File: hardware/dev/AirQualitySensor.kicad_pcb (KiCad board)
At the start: 2 copper layers, 81.3 x 36.8 mm, 44 parts, among them J1 USB_C_Receptacle_USB2.0, J2 SWD, J3 UART, U1 004-0-0053, U2 DHT22, U3 XC6206P332MR

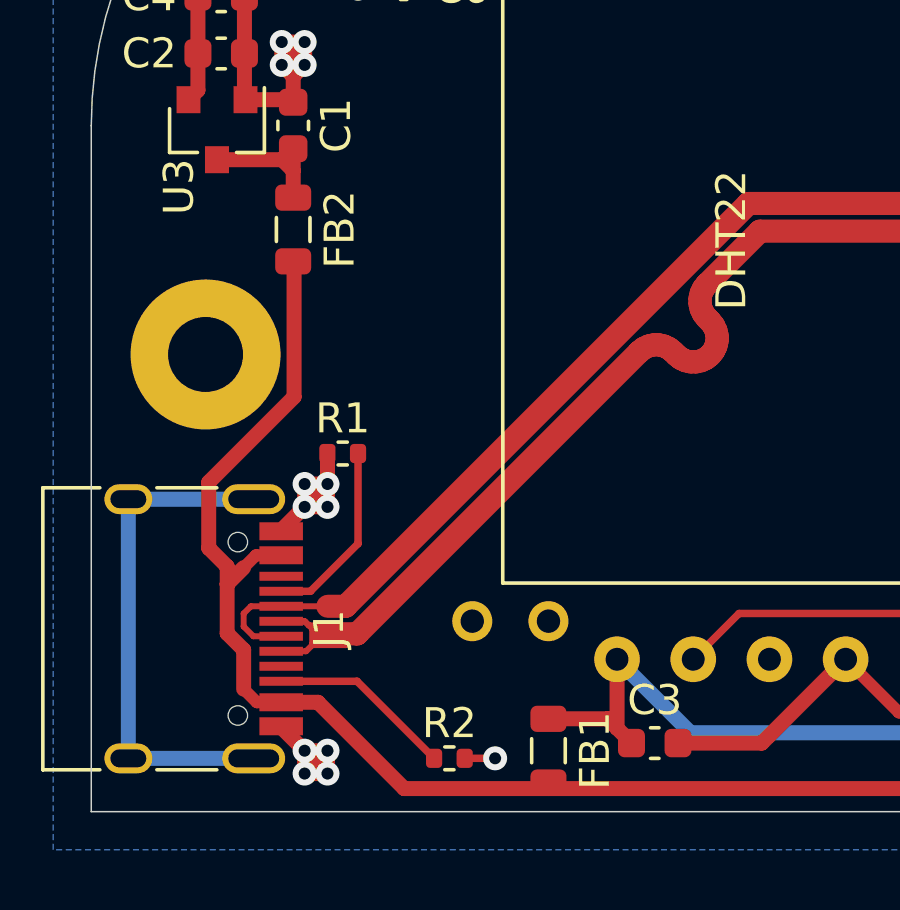
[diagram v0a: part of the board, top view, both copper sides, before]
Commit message: Fix inductor footprint
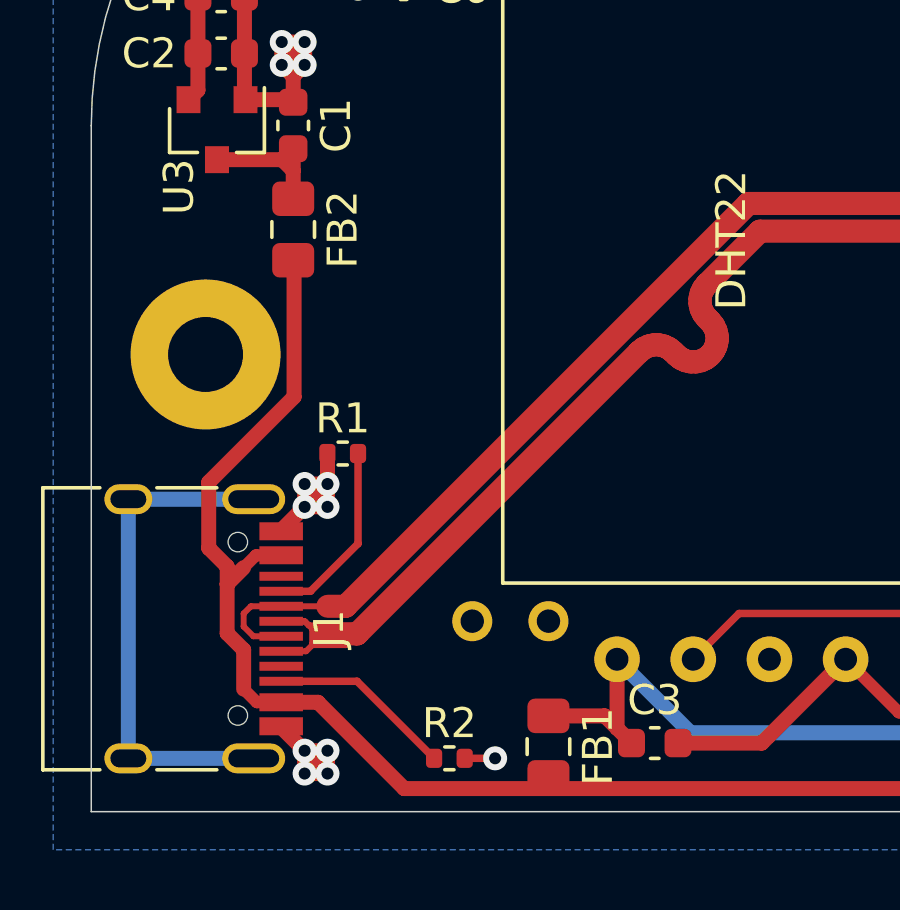
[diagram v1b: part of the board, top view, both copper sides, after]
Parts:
- FB1, FB2: footprint Inductor_SMD:L_0805_2012Metric -> Inductor_SMD:L_0805_2012Metric_Pad1.15x1.40mm_HandSolder
- moved FB1 0.14 mm to (121.9, 119.8)

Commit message: Fix flipped red-green LEDs
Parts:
- D1: value Red -> Green
- D3: value Green -> Red
- R6: value 10k -> 100k
- R8: value 100k -> 10k
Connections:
- A1 pad 7: LED_GREEN -> LED_RED
- A1 pad 9: LED_RED -> LED_GREEN
- R6 pad 2: LED_RED -> LED_GREEN
- R8 pad 2: LED_GREEN -> LED_RED
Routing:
- net LED_RED: track 12.5 -> 19.0 mm
- net LED_GREEN: track 19.0 -> 12.5 mm
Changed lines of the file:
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@@
   )
   (setup
-    (last_trace_width 0.5)
+    (last_trace_width 0.25)
     (user_trace_width 0.4)
     (user_trace_width 0.5)
@@
       (effects (font (size 1 1) (thickness 0.15)))
     )
-    (fp_text user %R (at 0 0 90) (layer F.Fab)
-      (effects (font (size 0.5 0.5) (thickness 0.08)))
-    )
     (fp_line (start -1 0.6) (end -1 -0.6) (layer F.Fab) (width 0.1))
     (fp_line (start -1 -0.6) (end 1 -0.6) (layer F.Fab) (width 0.1))
@@
     (fp_line (start 1.85 -0.95) (end 1.85 0.95) (layer F.CrtYd) (width 0.05))
     (fp_line (start 1.85 0.95) (end -1.85 0.95) (layer F.CrtYd) (width 0.05))
+    (fp_text user %R (at 0 0 90) (layer F.Fab)
+      (effects (font (size 0.5 0.5) (thickness 0.08)))
+    )
     (pad 2 smd roundrect (at 1.025 0 270) (size 1.15 1.4) (layers F.Cu F.Paste F.Mask) (roundrect_rratio 0.217391)
       (net 26 VBUS))
@@
     (fp_text value 100R (at 0 1.65 90) (layer F.Fab)
       (effects (font (size 1 1) (thickness 0.15)))
-    )
-    (fp_text user %R (at 0 0 90) (layer F.Fab)
-      (effects (font (size 0.5 0.5) (thickness 0.08)))
     )
     (fp_line (start -1 0.6) (end -1 -0.6) (layer F.Fab) (width 0.1))
@@
     (fp_line (start 1.85 -0.95) (end 1.85 0.95) (layer F.CrtYd) (width 0.05))
     (fp_line (start 1.85 0.95) (end -1.85 0.95) (layer F.CrtYd) (width 0.05))
+    (fp_text user %R (at 0 0 90) (layer F.Fab)
+      (effects (font (size 0.5 0.5) (thickness 0.08)))
+    )
     (pad 2 smd roundrect (at 1.025 0 270) (size 1.15 1.4) (layers F.Cu F.Paste F.Mask) (roundrect_rratio 0.217391)
       (net 26 VBUS))
@@
       (effects (font (size 1 1) (thickness 0.15)))
     )
-    (fp_text value 100k (at 0 1.17 90) (layer F.Fab)
+    (fp_text value 10k (at 0 1.17 90) (layer F.Fab)
       (effects (font (size 1 1) (thickness 0.15)))
     )
@@
     )
     (pad 2 smd roundrect (at 0.51 0 270) (size 0.54 0.64) (layers F.Cu F.Paste F.Mask) (roundrect_rratio 0.25)
-      (net 55 LED_GREEN))
+      (net 53 LED_RED))
     (pad 1 smd roundrect (at -0.51 0 270) (size 0.54 0.64) (layers F.Cu F.Paste F.Mask) (roundrect_rratio 0.25)
       (net 61 "Net-(D3-Pad2)"))
@@
       (effects (font (size 1 1) (thickness 0.15)))
     )
-    (fp_text value 10k (at 0 1.17 90) (layer F.Fab)
+    (fp_text value 100k (at 0 1.17 90) (layer F.Fab)
       (effects (font (size 1 1) (thickness 0.15)))
     )
@@
     )
     (pad 2 smd roundrect (at 0.51 0 270) (size 0.54 0.64) (layers F.Cu F.Paste F.Mask) (roundrect_rratio 0.25)
-      (net 53 LED_RED))
+      (net 55 LED_GREEN))
     (pad 1 smd roundrect (at -0.51 0 270) (size 0.54 0.64) (layers F.Cu F.Paste F.Mask) (roundrect_rratio 0.25)
       (net 59 "Net-(D1-Pad2)"))
@@
       (effects (font (size 1 1) (thickness 0.15)) (justify mirror))
     )
-    (fp_text value Green (at 1.27 -2.96 -90) (layer B.Fab)
+    (fp_text value Red (at 1.27 -2.96 -90) (layer B.Fab)
       (effects (font (size 1 1) (thickness 0.15)) (justify mirror))
     )
@@
       (effects (font (size 1 1) (thickness 0.15)) (justify mirror))
     )
-    (fp_text value Red (at 1.27 -2.96 -90) (layer B.Fab)
+    (fp_text value Green (at 1.27 -2.96 -90) (layer B.Fab)
       (effects (font (size 1 1) (thickness 0.15)) (justify mirror))
     )
@@
       (net 70 LED_STATUS0))
     (pad 9 smd roundrect (at -6.75 2.2 180) (size 1.53 0.67) (layers F.Cu F.Paste F.Mask) (roundrect_rratio 0.25)
-      (net 53 LED_RED))
+      (net 55 LED_GREEN))
     (pad 8 smd roundrect (at -6.75 1.1 180) (size 1.53 0.67) (layers F.Cu F.Paste F.Mask) (roundrect_rratio 0.25)
       (net 54 LED_YELLOW))
@@
       (net 48 SWD_SWCLK))
     (pad 7 smd roundrect (at -6.75 0 180) (size 1.53 0.67) (layers F.Cu F.Paste F.Mask) (roundrect_rratio 0.25)
-      (net 55 LED_GREEN))
+      (net 53 LED_RED))
   )
   (gr_text "PCB ID:" (at 133.35 109.22) (layer B.SilkS)
@@
   (segment (start 159.757553 114.590999) (end 155.214003 114.590999) (width 0.25) (layer F.Cu) (net 51))
   (segment (start 160.532 115.316) (end 160.482554 115.316) (width 0.25) (layer F.Cu) (net 51))
-  (via (at 150.368 100.076) (size 0.8) (drill 0.4) (layers F.Cu B.Cu) (net 53))
-  (segment (start 150.368 100.076) (end 150.368 99.062) (width 0.25) (layer F.Cu) (net 53))
-  (via (at 152.527 108.204) (size 0.8) (drill 0.4) (layers F.Cu B.Cu) (net 53))
-  (segment (start 151.482685 109.814) (end 151.022 109.814) (width 0.25) (layer F.Cu) (net 53))
-  (segment (start 152.527 108.769685) (end 151.482685 109.814) (width 0.25) (layer F.Cu) (net 53))
-  (segment (start 152.527 108.204) (end 152.527 108.769685) (width 0.25) (layer F.Cu) (net 53))
-  (segment (start 150.368 106.045) (end 150.368 100.076) (width 0.25) (layer B.Cu) (net 53))
-  (segment (start 152.527 108.204) (end 150.368 106.045) (width 0.25) (layer B.Cu) (net 53))
+  (via (at 150.368 100.076) (size 0.8) (drill 0.4) (layers F.Cu B.Cu) (net 55))
+  (segment (start 150.368 100.076) (end 150.368 99.062) (width 0.25) (layer F.Cu) (net 55))
+  (via (at 152.527 108.204) (size 0.8) (drill 0.4) (layers F.Cu B.Cu) (net 55))
+  (segment (start 151.482685 109.814) (end 151.022 109.814) (width 0.25) (layer F.Cu) (net 55))
+  (segment (start 152.527 108.769685) (end 151.482685 109.814) (width 0.25) (layer F.Cu) (net 55))
+  (segment (start 152.527 108.204) (end 152.527 108.769685) (width 0.25) (layer F.Cu) (net 55))
+  (segment (start 150.368 106.045) (end 150.368 100.076) (width 0.25) (layer B.Cu) (net 55))
+  (segment (start 152.527 108.204) (end 150.368 106.045) (width 0.25) (layer B.Cu) (net 55))
   (via (at 148.844 100.076) (size 0.8) (drill 0.4) (layers F.Cu B.Cu) (net 54))
   (segment (start 148.844 100.076) (end 148.844 99.062) (width 0.25) (layer F.Cu) (net 54))
@@
   (segment (start 149.91799 101.14999) (end 148.844 100.076) (width 0.25) (layer B.Cu) (net 54))
   (segment (start 149.91799 106.2314) (end 149.91799 101.14999) (width 0.25) (layer B.Cu) (net 54))
-  (via (at 147.32 100.076) (size 0.8) (drill 0.4) (layers F.Cu B.Cu) (net 55))
-  (segment (start 147.32 100.076) (end 147.32 99.062) (width 0.25) (layer F.Cu) (net 55))
-  (via (at 154.051 109.982) (size 0.8) (drill 0.4) (layers F.Cu B.Cu) (net 55))
-  (segment (start 152.019 112.014) (end 151.022 112.014) (width 0.25) (layer F.Cu) (net 55))
-  (segment (start 154.051 109.982) (end 152.019 112.014) (width 0.25) (layer F.Cu) (net 55))
-  (segment (start 154.051 109.982) (end 152.595588 109.982) (width 0.25) (layer B.Cu) (net 55))
-  (segment (start 152.595588 109.982) (end 151.351989 108.738401) (width 0.25) (layer B.Cu) (net 55))
-  (segment (start 151.351989 108.301809) (end 149.46798 106.4178) (width 0.25) (layer B.Cu) (net 55))
-  (segment (start 151.351989 108.738401) (end 151.351989 108.301809) (width 0.25) (layer B.Cu) (net 55))
-  (segment (start 149.46798 106.4178) (end 149.46798 101.33639) (width 0.25) (layer B.Cu) (net 55))
-  (segment (start 149.46798 101.33639) (end 148.932591 100.801001) (width 0.25) (layer B.Cu) (net 55))
-  (segment (start 147.770998 100.076) (end 147.32 100.076) (width 0.25) (layer B.Cu) (net 55))
-  (segment (start 148.495999 100.801001) (end 147.770998 100.076) (width 0.25) (layer B.Cu) (net 55))
-  (segment (start 148.932591 100.801001) (end 148.495999 100.801001) (width 0.25) (layer B.Cu) (net 55))
+  (via (at 147.32 100.076) (size 0.8) (drill 0.4) (layers F.Cu B.Cu) (net 53))
+  (segment (start 147.32 100.076) (end 147.32 99.062) (width 0.25) (layer F.Cu) (net 53))
+  (via (at 154.051 109.982) (size 0.8) (drill 0.4) (layers F.Cu B.Cu) (net 53))
+  (segment (start 152.019 112.014) (end 151.022 112.014) (width 0.25) (layer F.Cu) (net 53))
+  (segment (start 154.051 109.982) (end 152.019 112.014) (width 0.25) (layer F.Cu) (net 53))
+  (segment (start 154.051 109.982) (end 152.595588 109.982) (width 0.25) (layer B.Cu) (net 53))
+  (segment (start 152.595588 109.982) (end 151.351989 108.738401) (width 0.25) (layer B.Cu) (net 53))
+  (segment (start 151.351989 108.301809) (end 149.46798 106.4178) (width 0.25) (layer B.Cu) (net 53))
+  (segment (start 151.351989 108.738401) (end 151.351989 108.301809) (width 0.25) (layer B.Cu) (net 53))
+  (segment (start 149.46798 106.4178) (end 149.46798 101.33639) (width 0.25) (layer B.Cu) (net 53))
+  (segment (start 149.46798 101.33639) (end 148.932591 100.801001) (width 0.25) (layer B.Cu) (net 53))
+  (segment (start 147.770998 100.076) (end 147.32 100.076) (width 0.25) (layer B.Cu) (net 53))
+  (segment (start 148.495999 100.801001) (end 147.770998 100.076) (width 0.25) (layer B.Cu) (net 53))
+  (segment (start 148.932591 100.801001) (end 148.495999 100.801001) (width 0.25) (layer B.Cu) (net 53))
   (segment (start 176.53 106.68) (end 177.8 107.95) (width 0.25) (layer F.Cu) (net 59))
   (segment (start 176.53 101.41641) (end 176.53 106.68) (width 0.25) (layer F.Cu) (net 59))

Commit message: Fix clearance issue
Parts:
- moved FB2 0.36 mm to (113.4, 102.9)
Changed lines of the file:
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@@
     (thickness 1.6)
     (drawings 24)
-    (tracks 586)
+    (tracks 587)
     (zones 0)
     (modules 44)
@@
   )
   (setup
-    (last_trace_width 0.25)
+    (last_trace_width 0.5)
     (user_trace_width 0.4)
     (user_trace_width 0.5)
@@
   )
   (module Inductor_SMD:L_0805_2012Metric_Pad1.15x1.40mm_HandSolder (layer F.Cu)
-    (at 113.411 102.5145 270)
+    (at 113.411 102.87 270)
     (descr "Inductor SMD 0805 (2012 Metric), square (rectangular) end terminal, IPC_7351 nominal with elongated pad for handsoldering. (Body size source: https://docs.google.com/spreadsheets/d/1BsfQQcO9C6DZCsRaXUlFlo91Tg2WpOkGARC1WS5S8t0/edit?usp=sharing), generated with kicad-footprint-generator")
     (tags "inductor handsolder")
@@
   (segment (start 111.20999 114.33501) (end 111.20999 113.74999) (width 0.5) (layer F.Cu) (net 26))
   (segment (start 113.440001 103.606001) (end 113.411 103.577) (width 0.5) (layer F.Cu) (net 26))
-  (segment (start 113.440001 108.096001) (end 113.440001 103.606001) (width 0.5) (layer F.Cu) (net 26))
   (segment (start 121.92 121.142006) (end 121.912003 121.150003) (width 0.5) (layer F.Cu) (net 26))
   (segment (start 121.92 120.9505) (end 121.92 121.142006) (width 0.5) (layer F.Cu) (net 26))
+  (segment (start 113.440001 103.924001) (end 113.411 103.895) (width 0.5) (layer F.Cu) (net 26))
+  (segment (start 113.440001 108.096001) (end 113.440001 103.924001) (width 0.5) (layer F.Cu) (net 26))
   (segment (start 113.046 100.187) (end 113.411 99.822) (width 0.5) (layer F.Cu) (net 27))
   (segment (start 110.871 100.187) (end 113.046 100.187) (width 0.5) (layer F.Cu) (net 27))
   (segment (start 113.411 100.552) (end 113.046 100.187) (width 0.5) (layer F.Cu) (net 27))
-  (segment (start 113.411 99.822) (end 113.411 101.452) (width 0.5) (layer F.Cu) (net 27))
+  (segment (start 113.411 99.822) (end 113.411 101.845) (width 0.5) (layer F.Cu) (net 27))
   (segment (start 115.572 112.988) (end 115.572 109.982) (width 0.25) (layer F.Cu) (net 29))
   (segment (start 113.986 114.574) (end 115.572 112.988) (width 0.25) (layer F.Cu) (net 29))
